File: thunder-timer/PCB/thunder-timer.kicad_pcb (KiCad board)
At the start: 2 copper layers, 46 x 32 mm, 13 parts, among them J1 Conn_01x02, Q1 2PC945, SW1 SW_Push, U1 ATTINY85-20PU

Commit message: Added ground plane
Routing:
- added copper zone on B.Cu, net GND
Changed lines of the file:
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@@
     (links 14)
     (no_connects 0)
-    (area 89.924999 89.924999 136.075001 122.075001)
+    (area 81.942857 89.215 191.357142 122.075001)
     (thickness 1.6)
     (drawings 6)
@@
     (user_trace_width 0.5)
     (trace_clearance 0.2)
-    (zone_clearance 0.508)
+    (zone_clearance 0.5)
     (zone_45_only no)
     (trace_min 0.25)
@@
     (aux_axis_origin 0 0)
     (grid_origin 115.5 97.5)
-    (visible_elements 7FFEFFBF)
+    (visible_elements 7FFEFFFF)
     (pcbplotparams
       (layerselection 0x00030_80000001)
@@
   (segment (start 109.88 91.88) (end 108.12 91.88) (width 0.25) (layer B.Cu) (net 11))
   (segment (start 110.5 92.5) (end 109.88 91.88) (width 0.25) (layer B.Cu) (net 11))
+  (zone (net 2) (net_name GND) (layer B.Cu) (hatch edge 0.508)
+    (connect_pads (clearance 0.5))
+    (min_thickness 0.2)
+    (fill yes (arc_segments 32) (thermal_gap 0.508) (thermal_bridge_width 0.508))
+    (polygon
+      (pts
+        (xy 90 90) (xy 136 90) (xy 136 122) (xy 90 122)
+      )
+    )
+  )
 )

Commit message: Added more labels & logo on the silk screen.
The PCB is ready for production.
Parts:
- added REF***: OSHW-Logo2_7.3x6mm_SilkScreen, Symbols:OSHW-Logo2_7.3x6mm_SilkScreen, F.Cu at (95.0, 105.3)
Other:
- board text added: "Bottom"
- board text added: "OHL v1.2"
- board text added: "Rev. 18/1"
- board text added: "Thunder timer"
- board text added: "Top"
- board text added: "http://michis-pla.net"

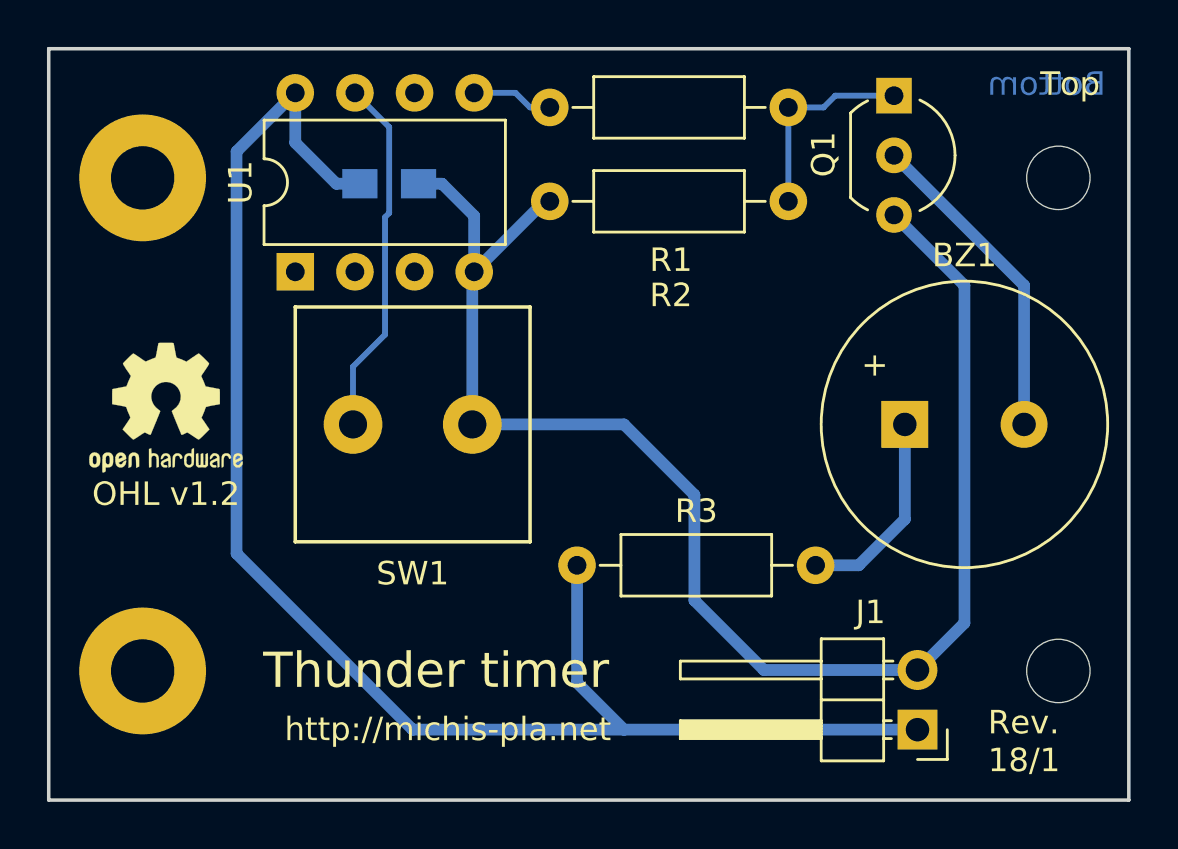
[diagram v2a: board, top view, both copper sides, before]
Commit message: Added a flyback diode since the standard buzzer is an inductive load.
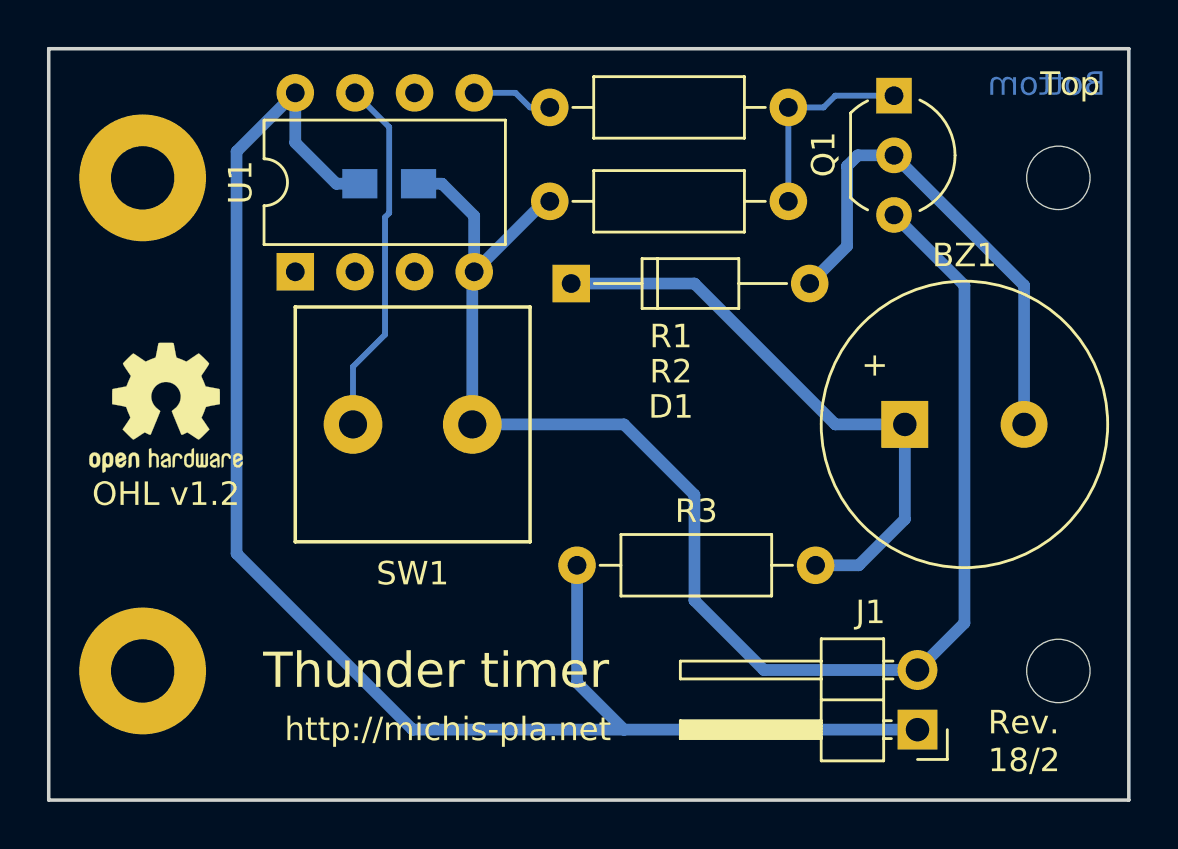
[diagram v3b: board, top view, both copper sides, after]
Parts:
- added D1: 1N4148, Diodes_THT:D_DO-35_SOD27_P10.16mm_Horizontal, F.Cu at (112.2, 100.0)
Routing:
- net Net-(BZ1-Pad1): track 8.65 -> 25.3 mm
- net Net-(BZ1-Pad2): track 13.8 -> 21.6 mm
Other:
- board text added: "Rev. 18/2"
- board text removed: "Rev. 18/1"
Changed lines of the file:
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@@
 (kicad_pcb (version 4) (host pcbnew 4.0.7)
   (general
-    (links 14)
+    (links 16)
     (no_connects 0)
-    (area 81.942857 89.215 191.357142 124.5)
+    (area 81.942857 89.215 191.357142 122.075001)
     (thickness 1.6)
     (drawings 12)
-    (tracks 43)
+    (tracks 50)
     (zones 0)
-    (modules 14)
+    (modules 15)
     (nets 12)
   )
@@
     (title thunder-timer)
     (date 2018-07-07)
-    (rev 1)
+    (rev 2)
     (company "Michael Bemmerl")
+    (comment 1 "Open Hardware: CERN OHL v1.2")
   )
   (layers
     (0 F.Cu signal)
-    (31 B.Cu signal hide)
+    (31 B.Cu signal)
     (32 B.Adhes user)
     (33 F.Adhes user)
@@
     (descr "Resistor, Axial_DIN0207 series, Axial, Horizontal, pin pitch=10.16mm, 0.25W = 1/4W, length*diameter=6.3*2.5mm^2, http://cdn-reichelt.de/documents/datenblatt/B400/1_4W%23YAG.pdf")
     (tags "Resistor Axial_DIN0207 series Axial Horizontal pin pitch 10.16mm 0.25W = 1/4W length 6.3mm diameter 2.5mm")
-    (fp_text reference R1 (at 5 -6.5 180) (layer F.SilkS)
+    (fp_text reference R1 (at 5 -9.75 180) (layer F.SilkS)
       (effects (font (size 1 1) (thickness 0.15)))
     )
@@
     (descr "Resistor, Axial_DIN0207 series, Axial, Horizontal, pin pitch=10.16mm, 0.25W = 1/4W, length*diameter=6.3*2.5mm^2, http://cdn-reichelt.de/documents/datenblatt/B400/1_4W%23YAG.pdf")
     (tags "Resistor Axial_DIN0207 series Axial Horizontal pin pitch 10.16mm 0.25W = 1/4W length 6.3mm diameter 2.5mm")
-    (fp_text reference R2 (at 5 -4 180) (layer F.SilkS)
+    (fp_text reference R2 (at 5 -7.25 180) (layer F.SilkS)
       (effects (font (size 1 1) (thickness 0.15)))
     )
@@
       (xy -0.113933 -2.757629) (xy -0.013056 -2.757714) (xy 0 -2.757714) (xy 0.10391 -2.757652)) (layer F.SilkS) (width 0.01))
   )
+  (module Diodes_THT:D_DO-35_SOD27_P10.16mm_Horizontal (layer F.Cu)
+    (at 112.25 100)
+    (descr "D, DO-35_SOD27 series, Axial, Horizontal, pin pitch=10.16mm, , length*diameter=4*2mm^2, , http://www.diodes.com/_files/packages/DO-35.pdf")
+    (tags "D DO-35_SOD27 series Axial Horizontal pin pitch 10.16mm  length 4mm diameter 2mm")
+    (fp_text reference D1 (at 4.25 5.25) (layer F.SilkS)
+      (effects (font (size 1 1) (thickness 0.15)))
+    )
+    (fp_text value 1N4148 (at 5.08 2.06) (layer F.Fab)
+      (effects (font (size 1 1) (thickness 0.15)))
+    )
+    (fp_text user %R (at 5.08 0) (layer F.Fab)
+      (effects (font (size 1 1) (thickness 0.15)))
+    )
+    (fp_line (start 3.08 -1) (end 3.08 1) (layer F.Fab) (width 0.1))
+    (fp_line (start 3.08 1) (end 7.08 1) (layer F.Fab) (width 0.1))
+    (fp_line (start 7.08 1) (end 7.08 -1) (layer F.Fab) (width 0.1))
+    (fp_line (start 7.08 -1) (end 3.08 -1) (layer F.Fab) (width 0.1))
+    (fp_line (start 0 0) (end 3.08 0) (layer F.Fab) (width 0.1))
+    (fp_line (start 10.16 0) (end 7.08 0) (layer F.Fab) (width 0.1))
+    (fp_line (start 3.68 -1) (end 3.68 1) (layer F.Fab) (width 0.1))
+    (fp_line (start 3.02 -1.06) (end 3.02 1.06) (layer F.SilkS) (width 0.12))
+    (fp_line (start 3.02 1.06) (end 7.14 1.06) (layer F.SilkS) (width 0.12))
+    (fp_line (start 7.14 1.06) (end 7.14 -1.06) (layer F.SilkS) (width 0.12))
+    (fp_line (start 7.14 -1.06) (end 3.02 -1.06) (layer F.SilkS) (width 0.12))
+    (fp_line (start 0.98 0) (end 3.02 0) (layer F.SilkS) (width 0.12))
+    (fp_line (start 9.18 0) (end 7.14 0) (layer F.SilkS) (width 0.12))
+    (fp_line (start 3.68 -1.06) (end 3.68 1.06) (layer F.SilkS) (width 0.12))
+    (fp_line (start -1.05 -1.35) (end -1.05 1.35) (layer F.CrtYd) (width 0.05))
+    (fp_line (start -1.05 1.35) (end 11.25 1.35) (layer F.CrtYd) (width 0.05))
+    (fp_line (start 11.25 1.35) (end 11.25 -1.35) (layer F.CrtYd) (width 0.05))
+    (fp_line (start 11.25 -1.35) (end -1.05 -1.35) (layer F.CrtYd) (width 0.05))
+    (pad 1 thru_hole rect (at 0 0) (size 1.6 1.6) (drill 0.8) (layers *.Cu *.Mask)
+      (net 9 "Net-(BZ1-Pad1)"))
+    (pad 2 thru_hole oval (at 10.16 0) (size 1.6 1.6) (drill 0.8) (layers *.Cu *.Mask)
+      (net 10 "Net-(BZ1-Pad2)"))
+    (model ${KISYS3DMOD}/Diodes_THT.3dshapes/D_DO-35_SOD27_P10.16mm_Horizontal.wrl
+      (at (xyz 0 0 0))
+      (scale (xyz 0.393701 0.393701 0.393701))
+      (rotate (xyz 0 0 0))
+    )
+  )
   (gr_text "OHL v1.2" (at 94.996 108.966) (layer F.SilkS)
     (effects (font (size 1 1) (thickness 0.15)))
   )
-  (gr_text "Rev.\n18/1" (at 130 119.5) (layer F.SilkS)
+  (gr_text "Rev.\n18/2" (at 130 119.5) (layer F.SilkS)
     (effects (font (size 1 1) (thickness 0.15)) (justify left))
   )
@@
   (segment (start 104.324 102.176) (end 102.96 103.54) (width 0.25) (layer B.Cu) (net 8))
   (segment (start 104.5 93.34) (end 104.5 97) (width 0.25) (layer B.Cu) (net 8))
+  (segment (start 112.25 100) (end 117.5 100) (width 0.5) (layer B.Cu) (net 9))
+  (segment (start 123.5 106) (end 126.46 106) (width 0.5) (layer B.Cu) (net 9))
+  (segment (start 117.5 100) (end 123.5 106) (width 0.5) (layer B.Cu) (net 9))
   (segment (start 122.66 112) (end 124.5 112) (width 0.5) (layer B.Cu) (net 9))
   (segment (start 126.46 110.04) (end 126.46 106) (width 0.5) (layer B.Cu) (net 9))
   (segment (start 124.5 112) (end 126.46 110.04) (width 0.5) (layer B.Cu) (net 9))
+  (segment (start 124 95) (end 124 98.41) (width 0.5) (layer B.Cu) (net 10))
+  (segment (start 124 95) (end 124.46 94.54) (width 0.5) (layer B.Cu) (net 10))
+  (segment (start 126 94.54) (end 124.46 94.54) (width 0.5) (layer B.Cu) (net 10))
+  (segment (start 124 98.41) (end 122.41 100) (width 0.5) (layer B.Cu) (net 10))
   (segment (start 131.54 106) (end 131.54 100.08) (width 0.5) (layer B.Cu) (net 10))
   (segment (start 131.54 100.08) (end 126 94.54) (width 0.5) (layer B.Cu) (net 10))

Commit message: I got the pin-out of Q1 wrong: It's ECB not BCE!
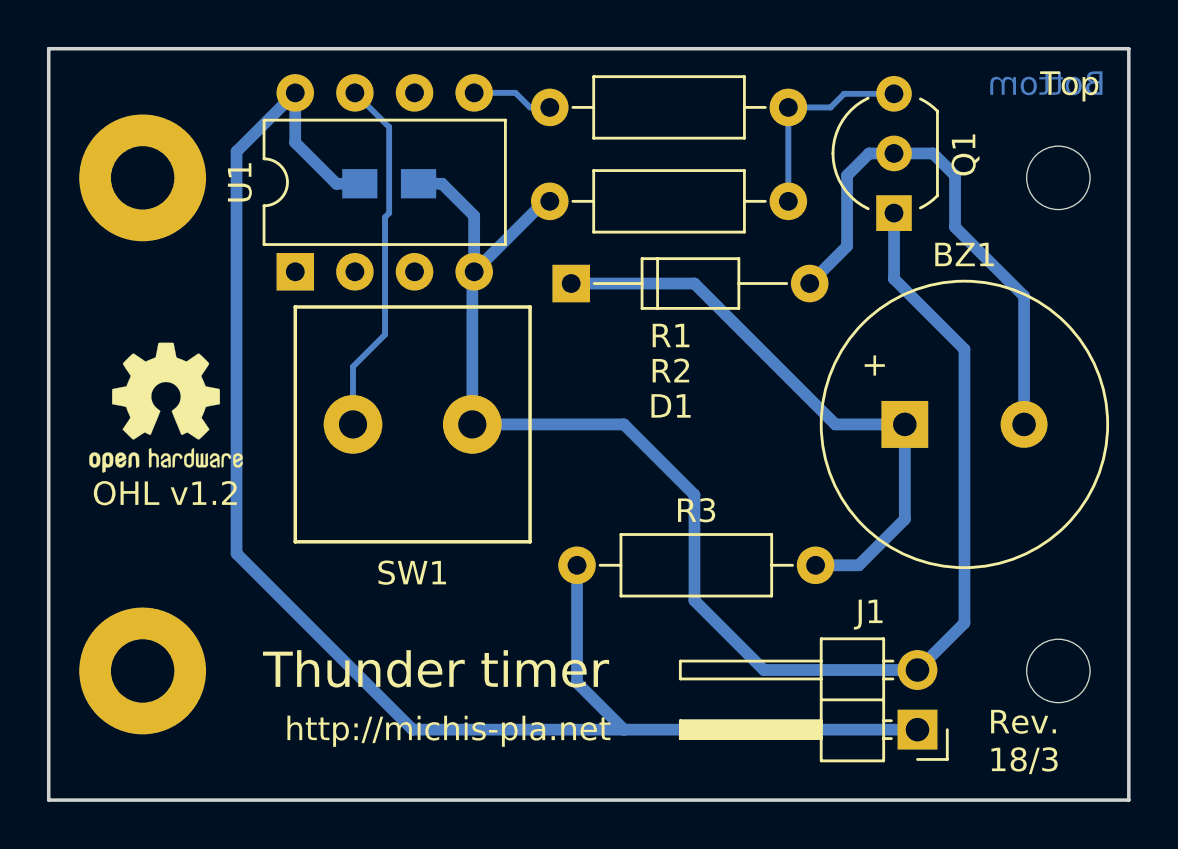
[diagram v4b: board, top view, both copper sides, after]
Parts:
- moved Q1 5.00 mm to (126.0, 97.0), turned to 90 degrees
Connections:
- Q1 pad 1: Net-(Q1-Pad1) -> GND
- Q1 pad 3: GND -> Net-(Q1-Pad3)
- R1 pad 1: Net-(Q1-Pad1) -> Net-(Q1-Pad3)
- R2 pad 1: Net-(Q1-Pad1) -> Net-(Q1-Pad3)
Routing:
- net Net-(Q1-Pad3): track 0.00 -> 8.74 mm
- net Net-(Q1-Pad1): track 8.71 -> 0.00 mm
- net Net-(BZ1-Pad2): track 21.6 -> 22.5 mm
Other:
- board text added: "Rev. 18/3"
- board text removed: "Rev. 18/2"

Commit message: Update to KiCad 5.
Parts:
- C1: footprint Capacitors_SMD:C_0805_HandSoldering -> Capacitor_SMD:C_0805_2012Metric_Pad1.15x1.40mm_HandSolder
- D1: footprint Diodes_THT:D_DO-35_SOD27_P10.16mm_Horizontal -> Diode_THT:D_DO-35_SOD27_P10.16mm_Horizontal
- J1: footprint Pin_Headers:Pin_Header_Angled_1x02_Pitch2.54mm -> Connector_PinHeader_2.54mm:PinHeader_1x02_P2.54mm_Horizontal
- Q1: footprint TO_SOT_Packages_THT:TO-92_Inline_Wide -> Package_TO_SOT_THT:TO-92L_Inline_Wide
- R1, R2, R3: footprint Resistors_THT:R_Axial_DIN0207_L6.3mm_D2.5mm_P10.16mm_Horizontal -> Resistor_THT:R_Axial_DIN0207_L6.3mm_D2.5mm_P10.16mm_Horizontal
- U1: footprint Housings_DIP:DIP-8_W7.62mm -> Package_DIP:DIP-8_W7.62mm
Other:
- board text added: "Rev. 19/4"
- board text removed: "Rev. 18/3"

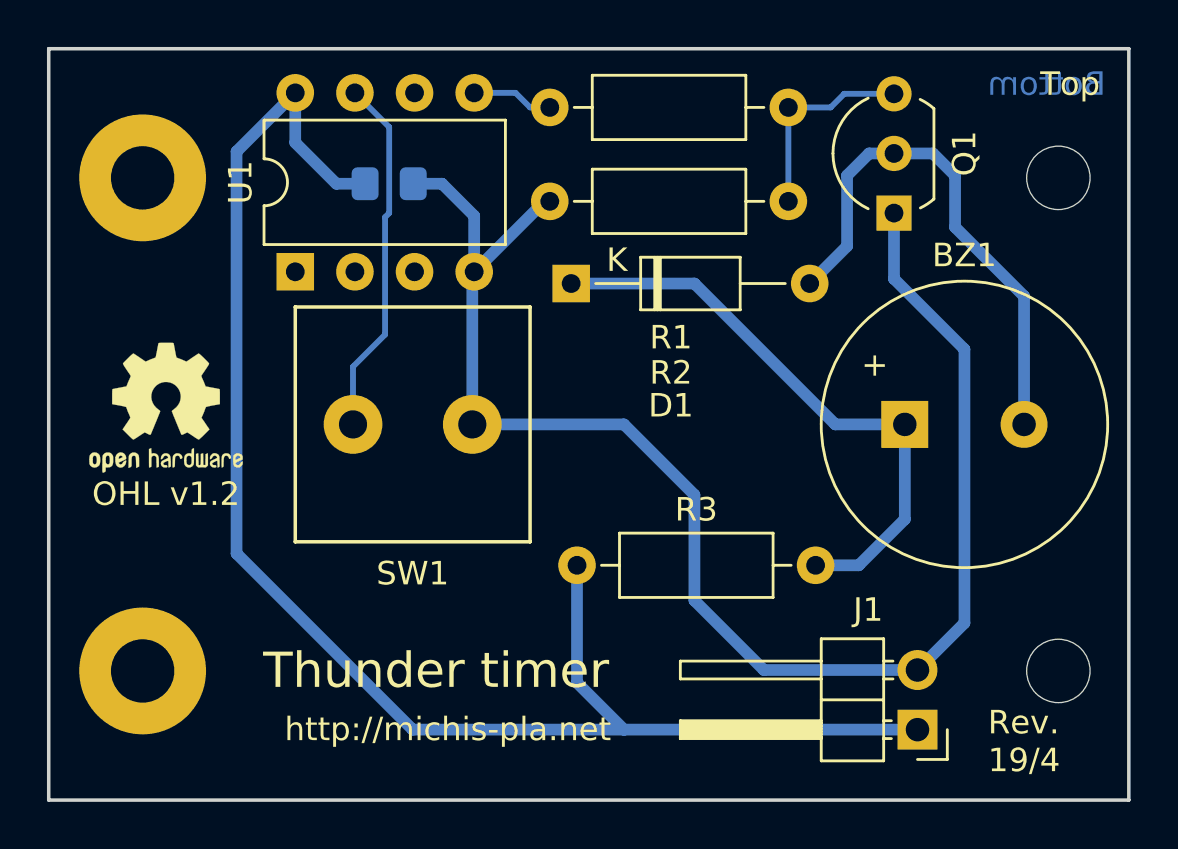
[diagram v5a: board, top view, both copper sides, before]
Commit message: Added a DC/DC converter to power the buzzer.
The nominal battery voltage of 2.4 is too less for adequately powering the 5 volt buzzer. The converter provides provides 5 volt exclusively for the buzzer and is enabled by the microcontroller.
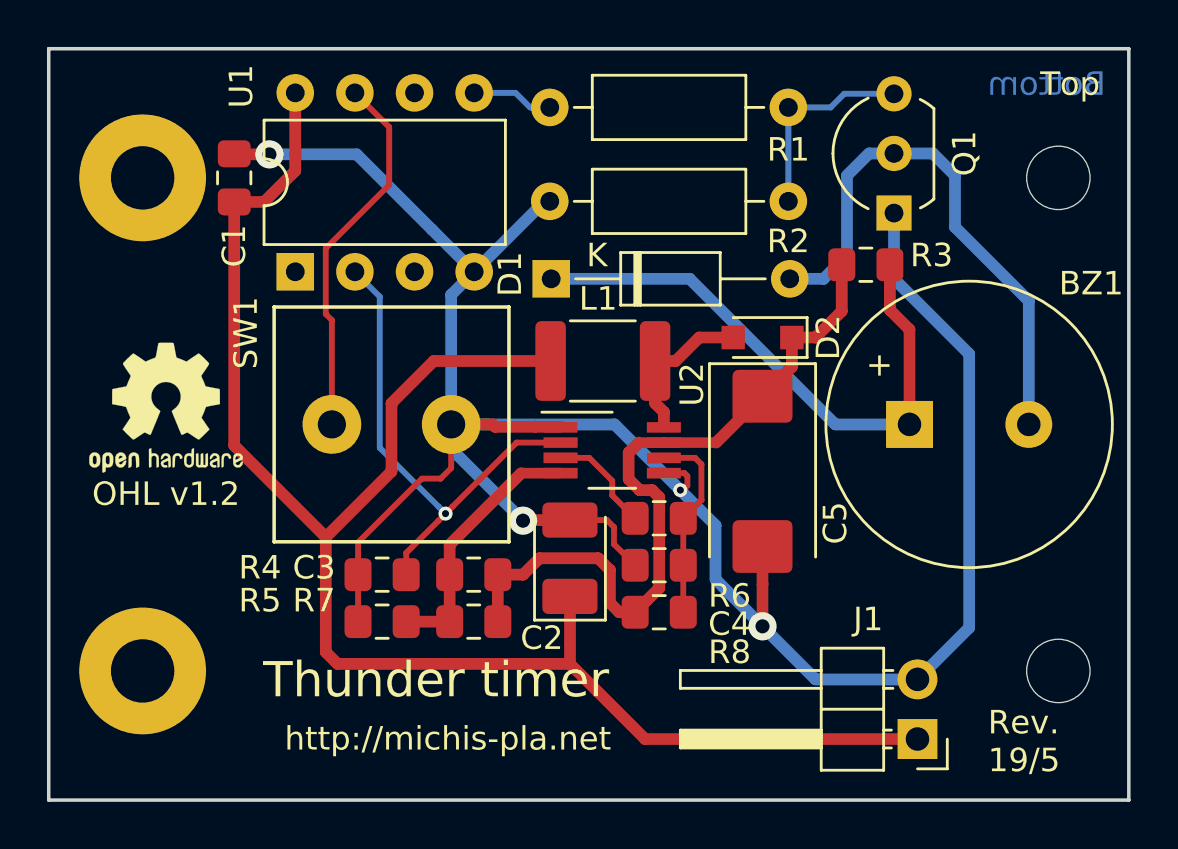
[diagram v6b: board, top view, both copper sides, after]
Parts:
- added C2: 22µ, Capacitor_Tantalum_SMD:CP_EIA-3528-21_Kemet-B_Pad1.50x2.35mm_HandSolder, F.Cu at (112.2, 111.7)
- added C3: 39p, Capacitor_SMD:C_0805_2012Metric_Pad1.15x1.40mm_HandSolder, F.Cu at (108.1, 112.4)
- added C4: 100n, Capacitor_SMD:C_0805_2012Metric_Pad1.15x1.40mm_HandSolder, F.Cu at (116.0, 112.0)
- added C5: 68µ, Capacitor_Tantalum_SMD:CP_EIA-7343-31_Kemet-D_Pad2.25x2.55mm_HandSolder, F.Cu at (120.4, 108.0)
- added D2: NSR0320MW2T1G, Diode_SMD:D_SOD-323_HandSoldering, F.Cu at (120.4, 102.3)
- added L1: 6µ8, Inductor_SMD:L_1812_4532Metric_Pad1.30x3.40mm_HandSolder, F.Cu at (113.6, 103.3)
- added R4: 100k, Resistor_SMD:R_0805_2012Metric_Pad1.15x1.40mm_HandSolder, F.Cu at (104.2, 112.4)
- added R5: 50k, Resistor_SMD:R_0805_2012Metric_Pad1.15x1.40mm_HandSolder, F.Cu at (104.2, 114.4)
- added R6: 200k, Resistor_SMD:R_0805_2012Metric_Pad1.15x1.40mm_HandSolder, F.Cu at (116.0, 110.0)
- added R7: 150k, Resistor_SMD:R_0805_2012Metric_Pad1.15x1.40mm_HandSolder, F.Cu at (108.1, 114.4)
- added R8: 500, Resistor_SMD:R_0805_2012Metric_Pad1.15x1.40mm_HandSolder, F.Cu at (116.0, 114.0)
- added U2: LM2621, Package_SO:VSSOP-8_3.0x3.0mm_P0.65mm, F.Cu at (114.0, 107.1)
- C1: moved to F.Cu
- R3: footprint Resistor_THT:R_Axial_DIN0207_L6.3mm_D2.5mm_P10.16mm_Horizontal -> Resistor_SMD:R_0805_2012Metric_Pad1.15x1.40mm_HandSolder
- moved R3 17.8 mm to (124.8, 99.2)
- moved C1 6.60 mm to (97.9, 95.5), turned to 90 degrees
- moved SW1 0.90 mm to (104.6, 106.0)
- moved D1 0.87 mm to (111.4, 99.8)
- moved J1 0.40 mm to (127.0, 119.4)
- moved BZ1 0.20 mm to (129.2, 106.0)
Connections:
- net Net-(R1-Pad2) renamed BUZ_PWM
- R3 pad 1: VCC -> +5V
- U1 pad 2: Net-(U1-Pad2) -> DCDC-PWR
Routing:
- net GND: track 63.8 -> 103.4 mm, vias 0 -> 4
- net +5V: track 0.00 -> 32.3 mm
- net DCDC-PWR: track 0.00 -> 21.3 mm, vias 0 -> 1
- net /FB: track 0.00 -> 11.1 mm
- net /DCDC-VCC: track 0.00 -> 8.33 mm
- net Net-(D2-Pad2): track 0.00 -> 6.69 mm
- net VCC: track 66.2 -> 71.2 mm
- net Net-(R6-Pad2): track 0.00 -> 4.61 mm
- net Net-(BZ1-Pad2): track 22.5 -> 23.5 mm
- net Net-(SW1-Pad2): track 15.4 -> 16.0 mm
- net Net-(BZ1-Pad1): track 25.3 -> 24.8 mm
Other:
- net class Default: via_drill 0.4 -> 0.3
- board text added: "Rev. 19/5"
- board text removed: "Rev. 19/4"
